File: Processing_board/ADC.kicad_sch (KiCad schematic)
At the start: 34 parts, among them U10 OPA192IDR, U11 REF5025AQDRQ1, U14 ADS7953SBDBT

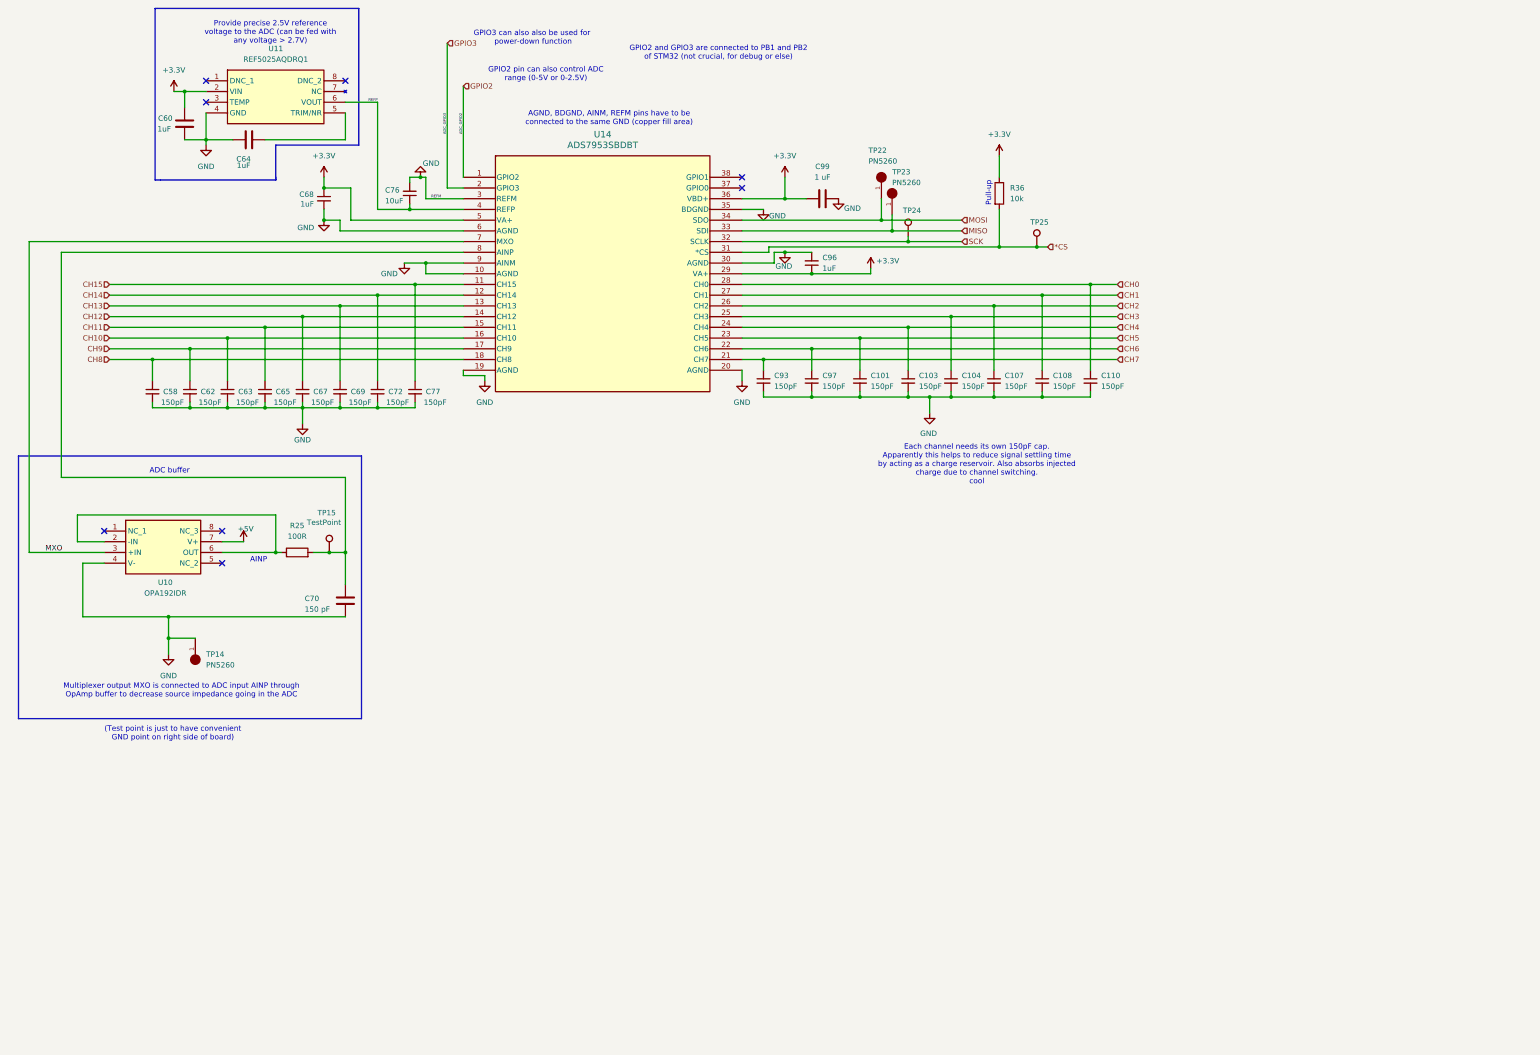
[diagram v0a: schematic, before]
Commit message: had to rename all components on the PCB to match the schematic
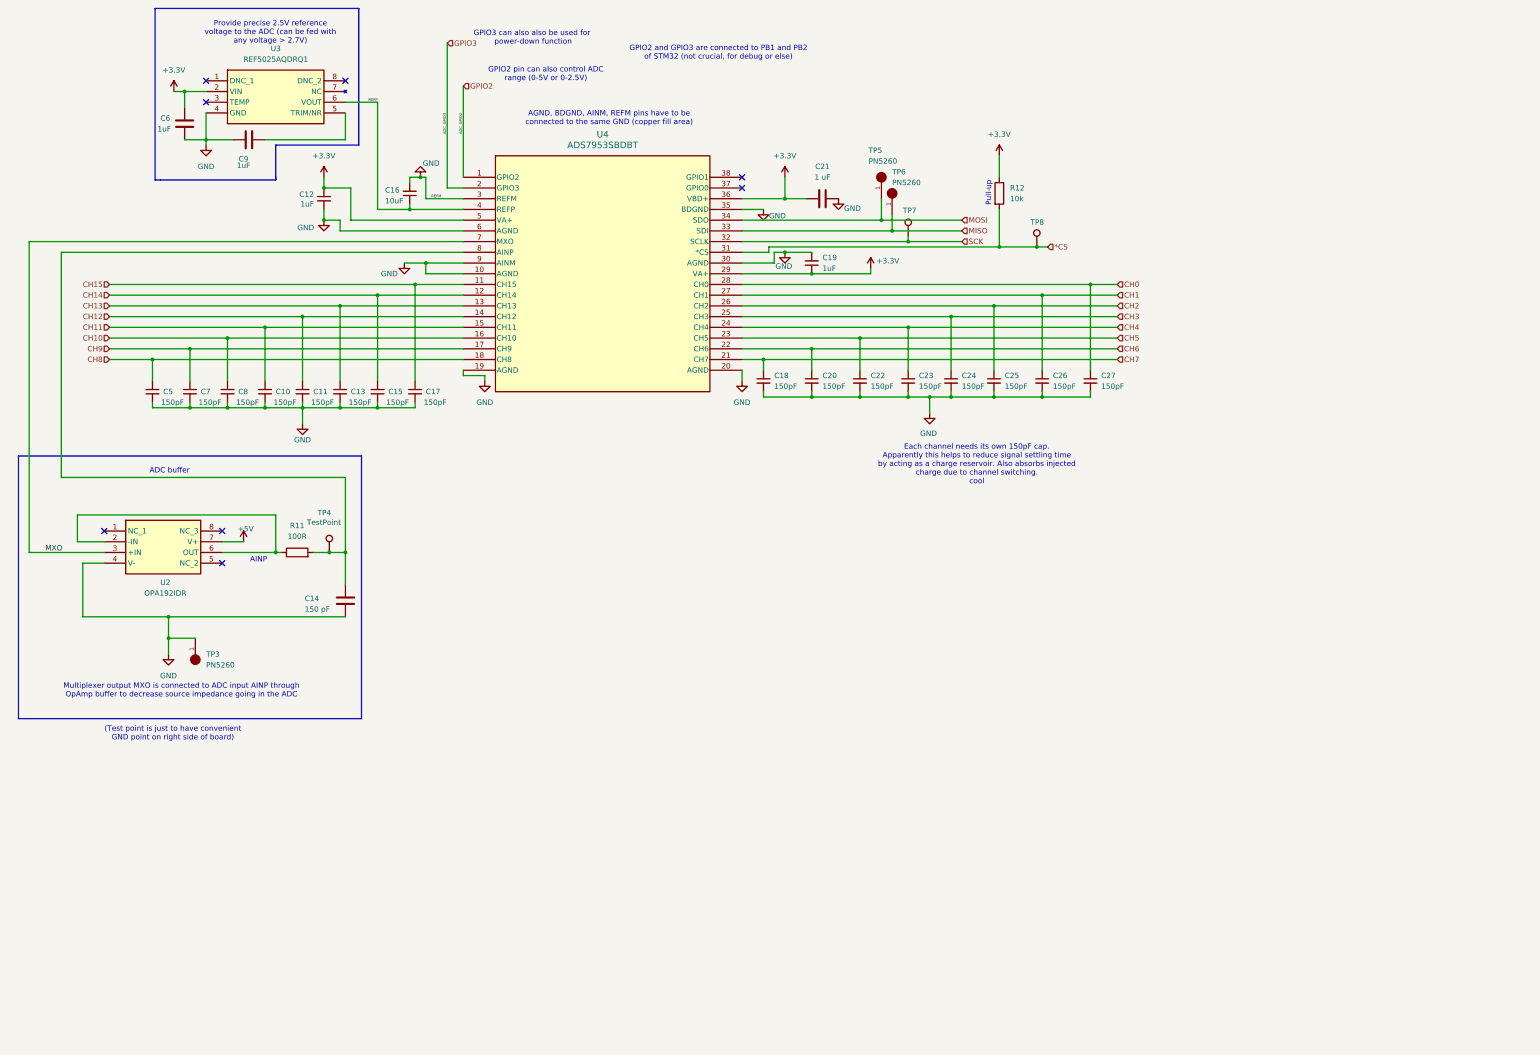
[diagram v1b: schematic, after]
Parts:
- renumbered C65 to C10, C67 to C11, C68 to C12, C69 to C13, C70 to C14, C72 to C15, C76 to C16, C77 to C17, C93 to C18, C96 to C19, C97 to C20, C99 to C21, C101 to C22, C103 to C23, C104 to C24, C107 to C25, C108 to C26, C110 to C27, C58 to C5, C60 to C6, C62 to C7, C63 to C8, C64 to C9, R25 to R11, R36 to R12, TP14 to TP3, TP15 to TP4, TP22 to TP5, TP23 to TP6, TP24 to TP7, TP25 to TP8, U10 to U2, U11 to U3, U14 to U4

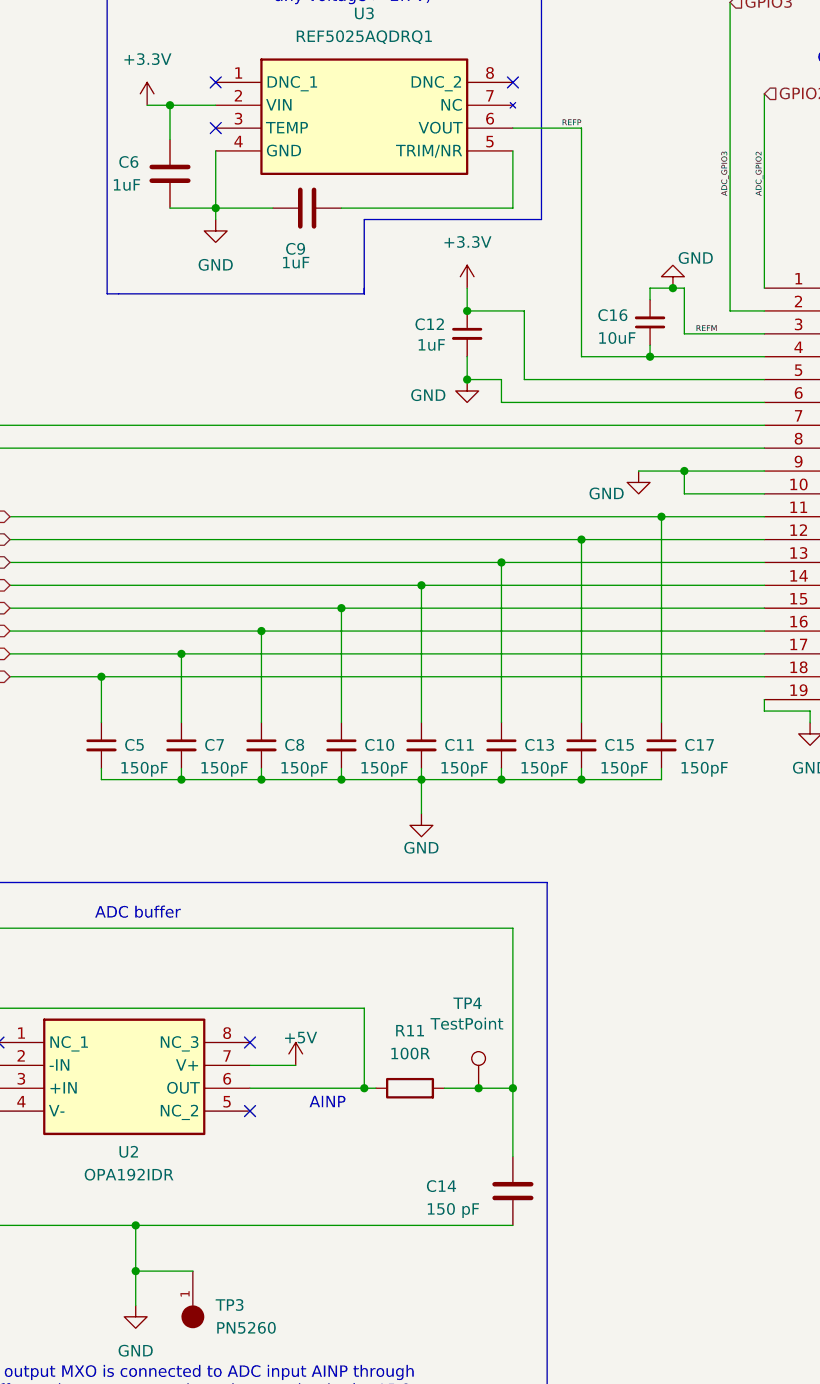
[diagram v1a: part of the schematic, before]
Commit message: created BOM, deleted useless folder Components and renamed CAD_Models to Parts
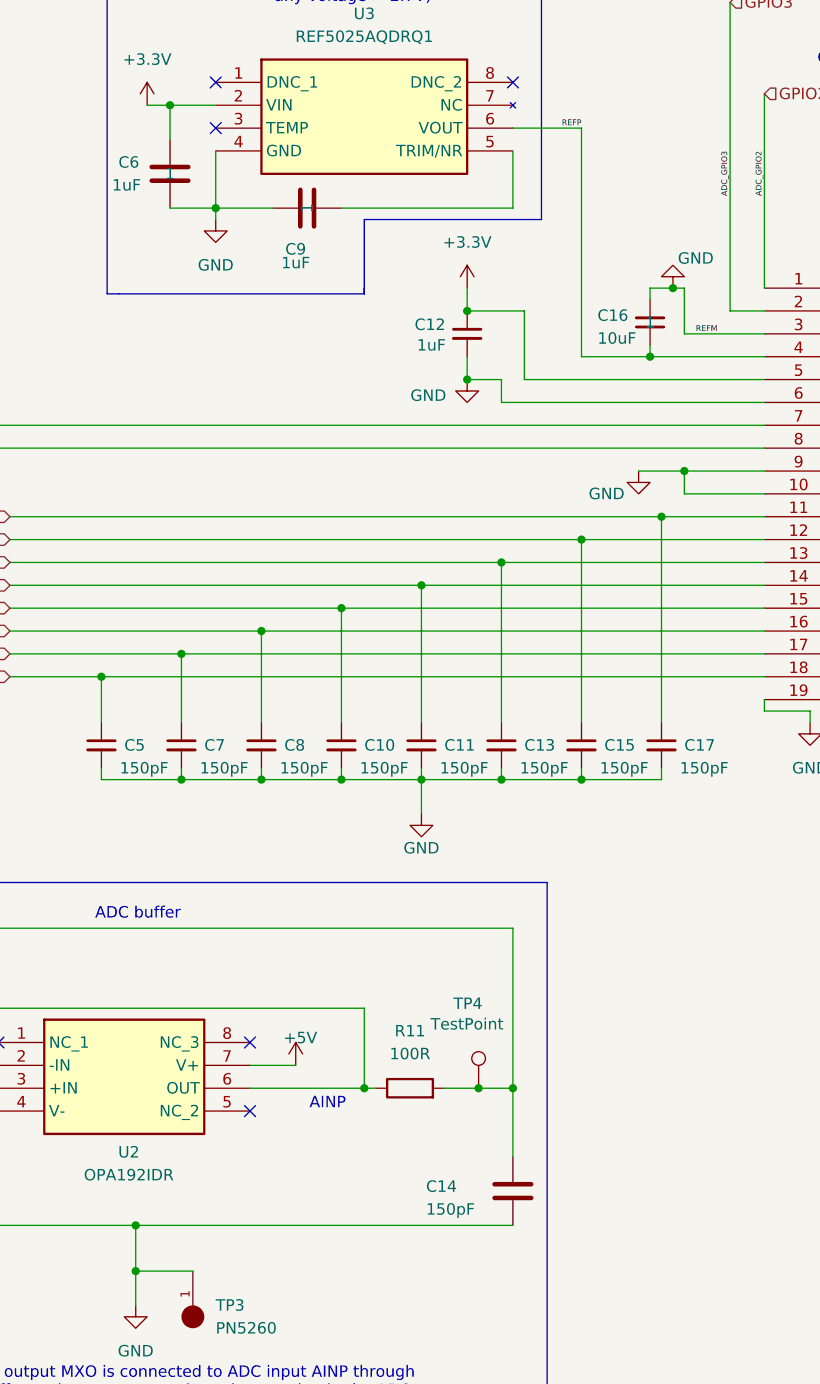
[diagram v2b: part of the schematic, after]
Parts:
- C10, C11, C13, C15, C17, C18, C20, C22, C23, C24, C25, C26, C27, C5, C7, C8: Link (none) -> https://www.mouser.ch/ProductDetail/KEMET/C0402C151K5RACTU?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; MANUFACTURER (none) -> KEMET; Manufacturer_Part_Number (none) -> C0402C151K5RACTU; Panier (none) -> 1
- C12, C19, C6, C9: Link (none) -> https://www.mouser.ch/ProductDetail/Samsung-Electro-Mechani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; MANUFACTURER (none) -> Samsung Electro-Mechanics; Manufacturer_Part_Number (none) -> CL05A105KP5NNNC; Panier (none) -> 1
- C14: value 150 pF -> 150pF; Link (none) -> https://www.mouser.ch/ProductDetail/KEMET/C0402C151K5RACTU?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; MANUFACTURER (none) -> KEMET; Manufacturer_Part_Number (none) -> C0402C151K5RACTU; Panier (none) -> 1
- C16: Link (none) -> https://www.mouser.ch/ProductDetail/Murata-Electronics/GRM1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; MANUFACTURER (none) -> Murata Electronics; Manufacturer_Part_Number (none) -> GRM155R61A106ME11D; Panier (none) -> 1
- C21: Link (none) -> https://www.mouser.ch/ProductDetail/Samsung-Electro-Mechani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; MANUFACTURER (none) -> Samsung Electro-Mechanics; Manufacturer_Part_Number (none) -> CL05A105KP5NNNC; déjà (none) -> 1
- R11: Link (none) -> https://www.mouser.ch/ProductDetail/KOA-Speer/RK73B1ETTPD10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; MANUFACTURER (none) -> KOA Speer; Manufacturer_Part_Number (none) -> RK73B1ETTPD101J; Panier (none) -> 1
- R12: Link (none) -> https://www.mouser.ch/ProductDetail/Wurth-Elektronik/560112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; MANUFACTURER (none) -> Wurth Elektronik; Manufacturer_Part_Number (none) -> 560112110020; Panier (none) -> 1
- TP3, TP5, TP6: Link (none) -> https://www.mouser.ch/ProductDetail/Keystone-Electronics/52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; Manufacturer_Part_Number (none) -> 5260; Panier (none) -> 1
- U2: Link (none) -> https://www.mouser.ch/ProductDetail/Texas-Instruments/OPA19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; MANUFACTURER (none) -> TI; Panier (none) -> 1
- U3: Link (none) -> https://www.mouser.ch/ProductDetail/Texas-Instruments/REF50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; MANUFACTURER (none) -> TI; déjà (none) -> 1
- U4: Link (none) -> https://www.mouser.ch/ProductDetail/Texas-Instruments/ADS79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; MANUFACTURER (none) -> TI; Manufacturer_Part_Number (none) -> ADS7953SBDBT; déjà (none) -> 1

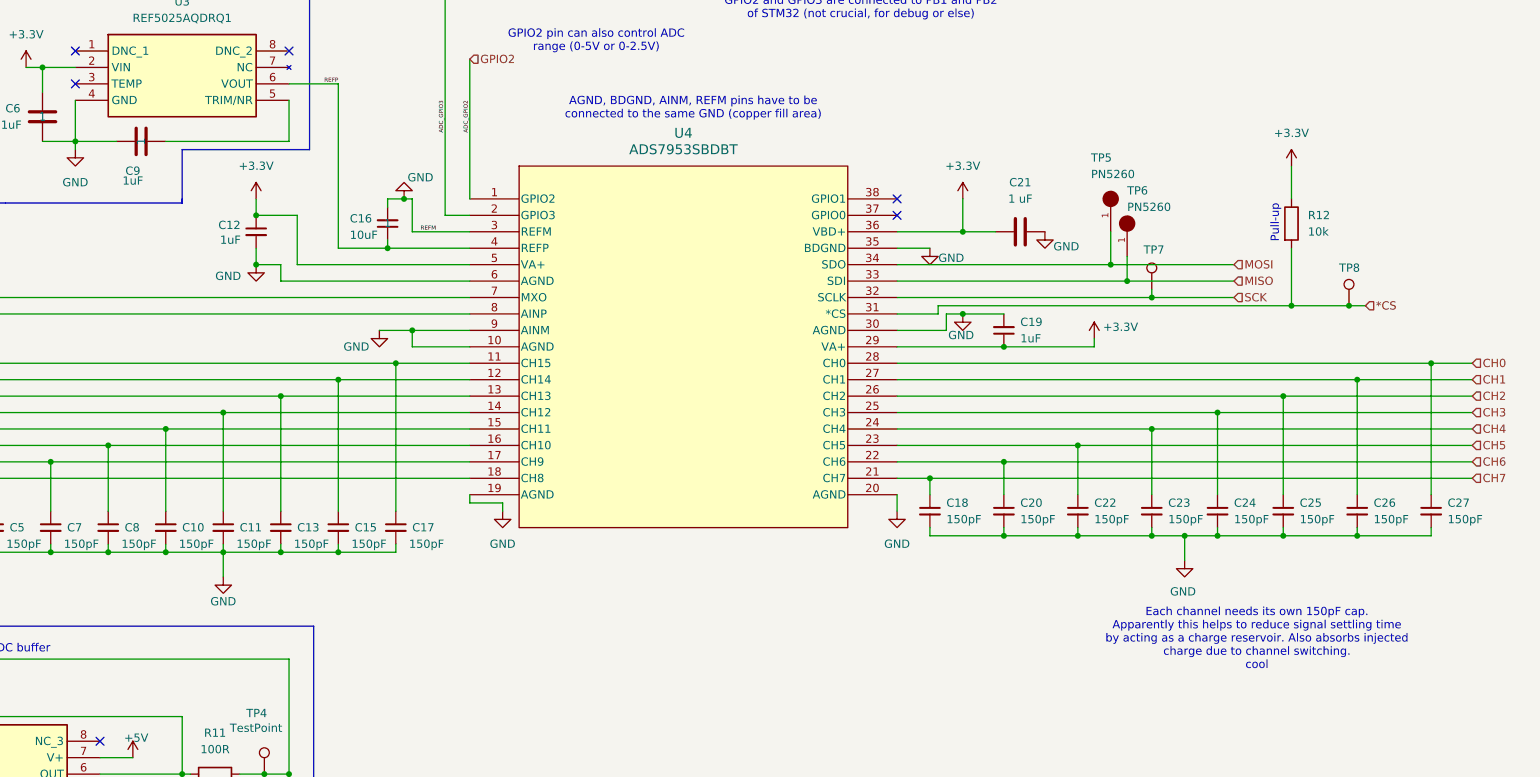
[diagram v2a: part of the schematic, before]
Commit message: correct text height/width for silkscreen, correct 3D models for THT pin headers
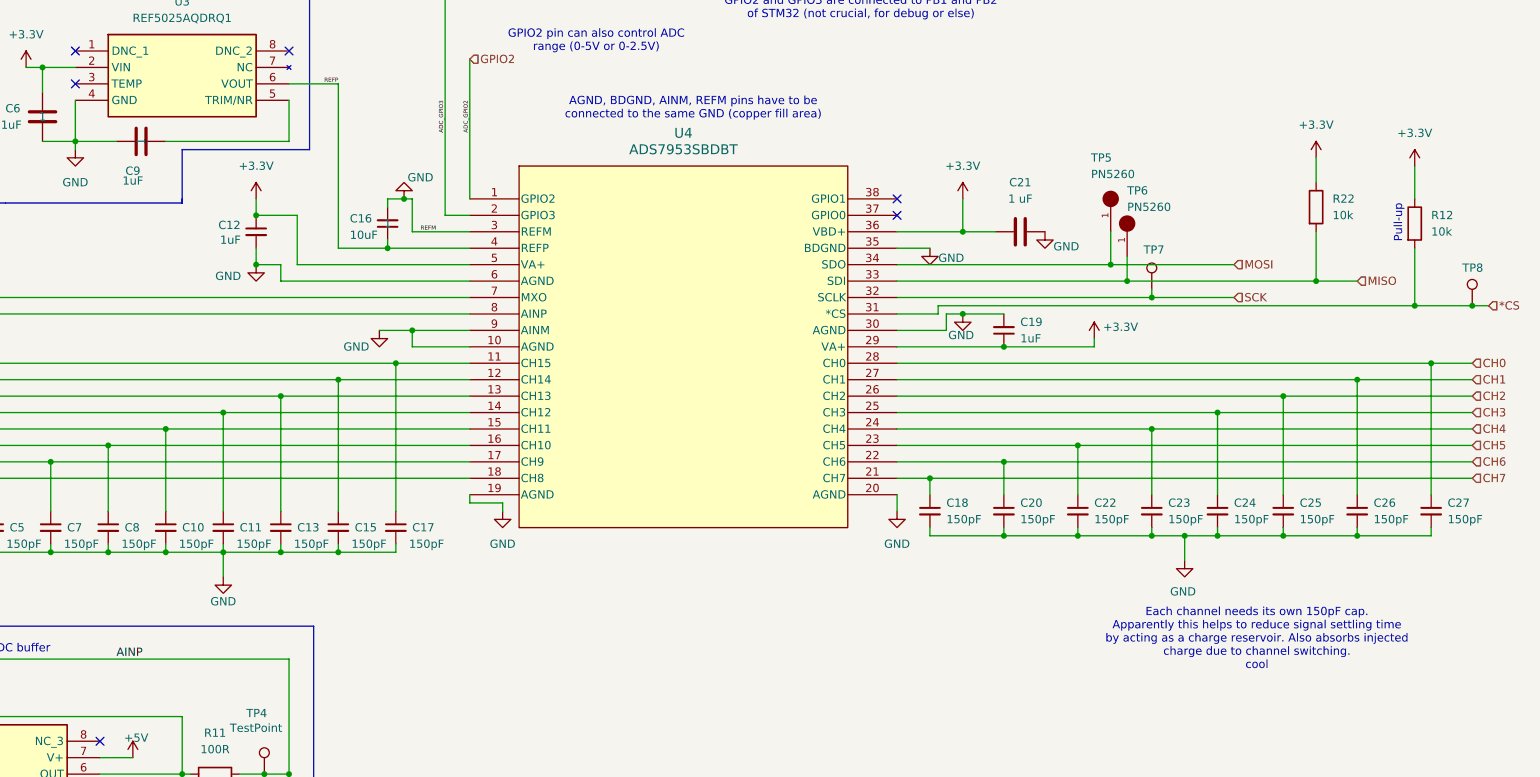
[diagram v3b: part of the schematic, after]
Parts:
- added R22: 10k, Resistor_SMD:R_0402_1005Metric, symbol Device:R
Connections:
- net +3.3V: now also R22.1
- net MISO: now also R22.2
- net AINP: now reaches C14.1, R11.2, TP4.1, U4.8 (AINP)
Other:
- moved on the sheet: R12, TP8

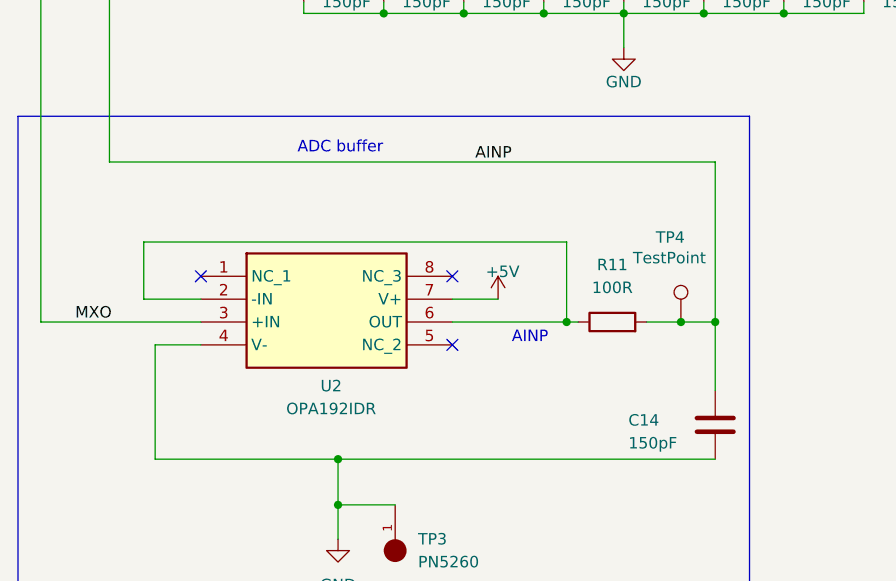
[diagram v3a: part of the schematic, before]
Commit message: add 100nF to OPA192 power pin
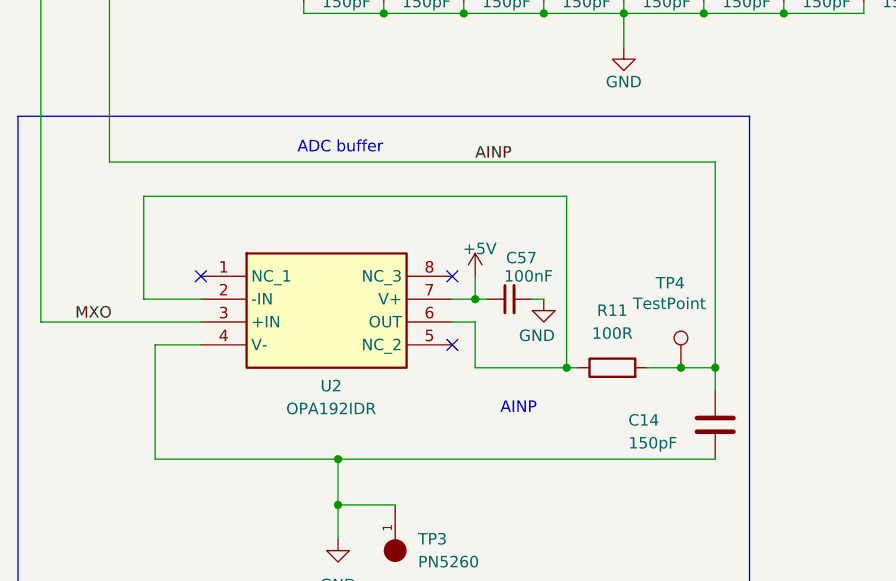
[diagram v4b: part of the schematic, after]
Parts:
- added C57: 100nF, Capacitor_SMD:C_0402_1005Metric, symbol Device:C_Small
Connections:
- net +5V: now also C57.1
- net GND: now also C57.2
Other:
- moved on the sheet: R11, TP4

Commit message: added Block Diagram (in KiCad and PDF) ; minor silkscreen cleanup
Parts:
- C57: Link https://www.mouser.ch/ProductDetail/Samsung-Electro-Mechani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 -> https://eu.mouser.com/ProductDetail/Samsung-Electro-Mechani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; Manufacturer_Part_Number CL05A105KP5NNNC -> CL05B104KP5VPNC
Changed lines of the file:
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@@
 			)
 		)
-		(property "Link" "https://www.mouser.ch/ProductDetail/Samsung-Electro-Mechanics/CL05A105KP5NNNC?qs=X6jEic%2FHinBsUeNeR9HD7w%3D%3D"
+		(property "Link" "https://eu.mouser.com/ProductDetail/Samsung-Electro-Mechanics/CL05B104KP5VPNC?qs=gqBM4hNBiUXTv%252BkFO9q2pQ%3D%3D"
 			(at 69.85 139.7 0)
 			(effects
@@
 			)
 		)
-		(property "Manufacturer_Part_Number" "CL05A105KP5NNNC"
+		(property "Manufacturer_Part_Number" "CL05B104KP5VPNC "
 			(at 69.85 139.7 0)
 			(effects
